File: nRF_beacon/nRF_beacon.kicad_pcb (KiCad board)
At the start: 2 copper layers, 22 parts, among them U1 nRF54L15-QFAA, U2 NPM1300-QEAA-R7, U3 MAX98357A, X1 32MHz

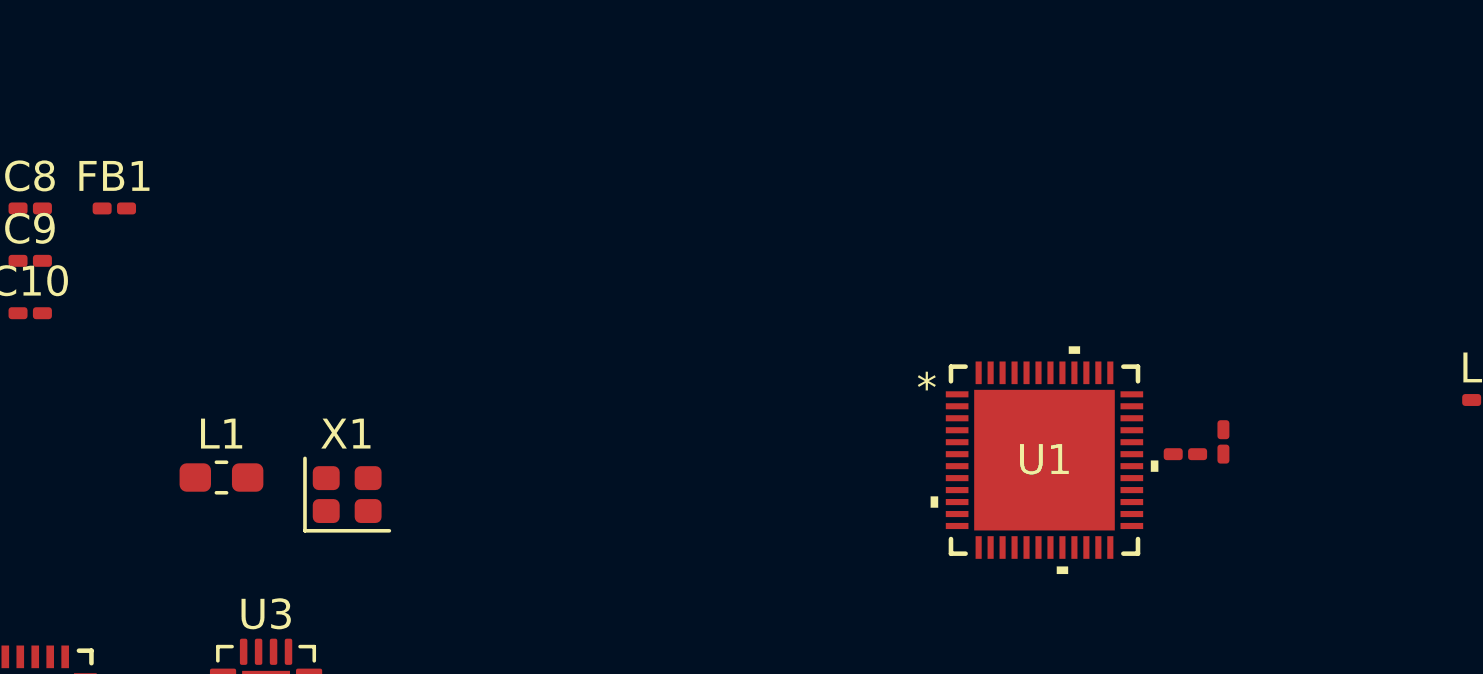
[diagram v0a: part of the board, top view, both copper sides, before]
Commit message: Updated nPM schematic. Added TWI and debug connector
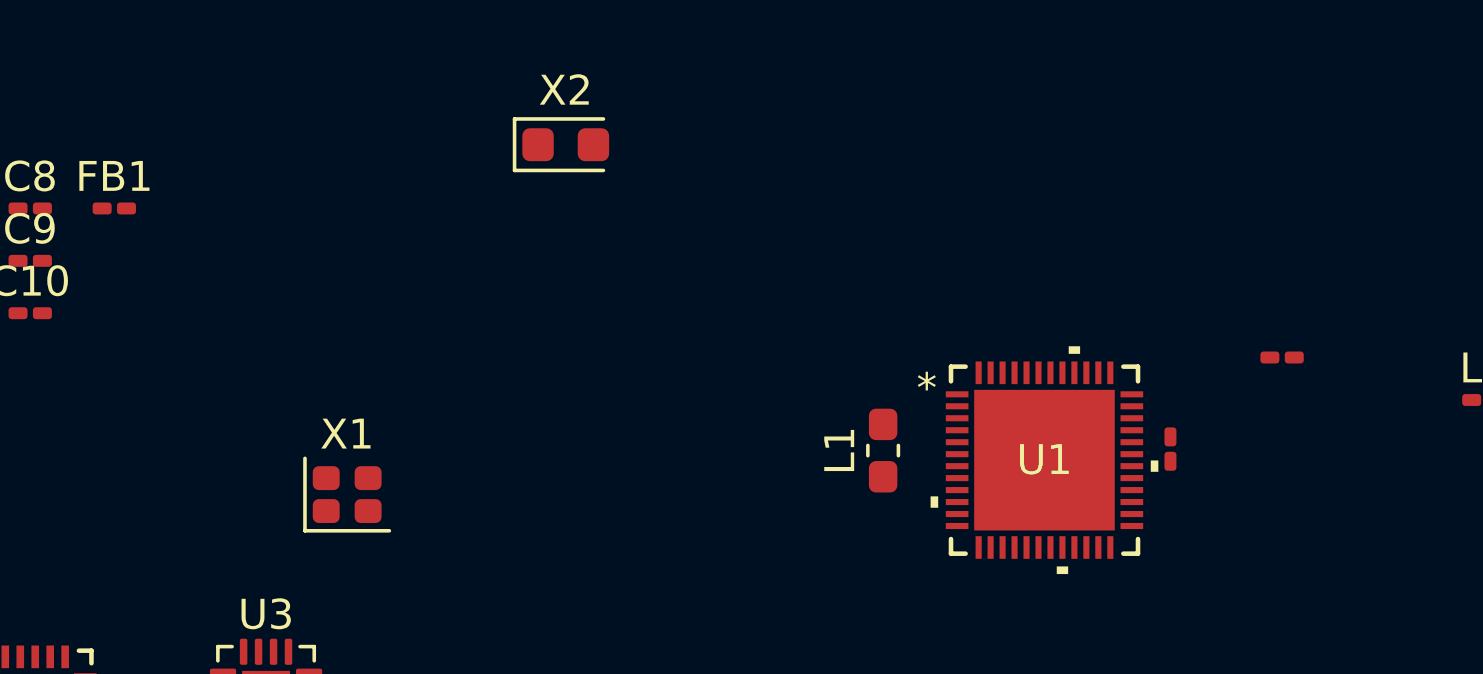
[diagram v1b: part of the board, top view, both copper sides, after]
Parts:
- added X2: 32.768 kHz, Crystal:Crystal_SMD_2012-2Pin_2.0x1.2mm_HandSoldering, F.Cu at (153.0, 64.5)
- moved L1 22.1 mm to (163.6, 74.7), turned to 90 degrees
- moved L2 4.57 mm to (176.9, 71.6)
- moved C11 1.79 mm to (173.2, 74.7)
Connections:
- net /~{SD_MODE} renamed Net-(U3-~{SD_MODE})
- net PVSS1 renamed Net-(U2-PVSS1)
- U1 pad 1: unconnected-(U1C-P1.00/XL1-Pad1) -> Net-(U1C-P1.00/XL1)
- U1 pad 2: unconnected-(U1C-P1.01/XL2-Pad2) -> Net-(U1C-P1.01/XL2)
- U1 pad 39: unconnected-(U1C-P1.11/AIN4/CK-Pad39) -> /MCU/SDA
- U1 pad 40: unconnected-(U1C-P1.12/AIN5/CK-Pad40) -> /MCU/SCL
- U1 pad 6: /DIN -> /LRCLK
- U1 pad 7: /LRCLK -> /DIN/DOUT
- U1 pad 8: /MCU/P1.07/AIN3 -> unconnected-(U1C-P1.07/AIN3-Pad8)
- U2 pad 1: VOUT1 -> VDD_AUDIO
- U2 pad 12: unconnected-(U2-VDDIO-Pad12) -> VDD_nRF
- U2 pad 13: unconnected-(U2-SDA-Pad13) -> /MCU/SDA
- U2 pad 14: unconnected-(U2-SCL-Pad14) -> /MCU/SCL
- U2 pad 21: /POWER/VBUS -> unconnected-(U2-VBUS-Pad21)
- U2 pad 23: /POWER/CC1 -> unconnected-(U2-CC1-Pad23)
- U2 pad 24: /POWER/CC2 -> unconnected-(U2-CC2-Pad24)
- U2 pad 29: (no net) -> unconnected-(U2-LSOUT1/VOUTLDO1-Pad29)
- U2 pad 32: unconnected-(U2-VOUT2-Pad32) -> VDD_nRF
- U2 pad 33: unconnected-(U2-AVSS-Pad33) -> Earth
- U2 pad 5: unconnected-(U2-SW2-Pad5) -> /POWER/SW2
- U2 pad 6: unconnected-(U2-PVSS2-Pad6) -> PVSS2
- U3 pad 1: /DIN -> /DIN/DOUT
- U3 pad 7: +5V -> VDD_AUDIO
- U3 pad 8: +5V -> VDD_AUDIO

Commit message: Finished first schematic draft. Ready for layout
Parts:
- added AE1: Antenna, Ekse:PCB_Antenna, F.Cu at (207.5, 61.6)
- added C14: 10uF, Capacitor_SMD:C_0603_1608Metric_Pad1.08x0.95mm_HandSolder, F.Cu at (149.5, 140.7)
- added C15: 2.2uF, Capacitor_SMD:C_0603_1608Metric_Pad1.08x0.95mm_HandSolder, F.Cu at (149.5, 143.2)
- added C16: 10uF, Capacitor_SMD:C_0603_1608Metric_Pad1.08x0.95mm_HandSolder, F.Cu at (149.5, 145.7)
- added C17: 10uF, Capacitor_SMD:C_0603_1608Metric_Pad1.08x0.95mm_HandSolder, F.Cu at (161.2, 140.7)
- added C18: 0.1uF, Capacitor_SMD:C_0201_0603Metric_Pad0.64x0.40mm_HandSolder, F.Cu at (164.8, 146.4)
- added C19: 220pF, Capacitor_SMD:C_0603_1608Metric_Pad1.08x0.95mm_HandSolder, F.Cu at (161.2, 143.2)
- added C20: 220pF, Capacitor_SMD:C_0603_1608Metric_Pad1.08x0.95mm_HandSolder, F.Cu at (161.2, 145.7)
- added C21: 0.1uF, Capacitor_SMD:C_0201_0603Metric_Pad0.64x0.40mm_HandSolder, F.Cu at (202.8, 129.2)
- added C22: 0.1uF, Capacitor_SMD:C_0201_0603Metric_Pad0.64x0.40mm_HandSolder, F.Cu at (153.1, 147.0)
- added C23: 10uF, Capacitor_SMD:C_0603_1608Metric_Pad1.08x0.95mm_HandSolder, F.Cu at (149.5, 148.3)
- added C24: 10uF, Capacitor_SMD:C_0603_1608Metric_Pad1.08x0.95mm_HandSolder, F.Cu at (149.5, 150.8)
- added C25: 10uF, Capacitor_SMD:C_0603_1608Metric_Pad1.08x0.95mm_HandSolder, F.Cu at (149.5, 153.3)
- added D1: LED_RGBA, Ekse:APGF1012GBRC07, F.Cu at (153.8, 153.5)
- added FB2: 1000, Capacitor_SMD:C_0805_2012Metric_Pad1.18x1.45mm_HandSolder, F.Cu at (165.8, 141.0)
- added FB3: 1000, Capacitor_SMD:C_0805_2012Metric_Pad1.18x1.45mm_HandSolder, F.Cu at (165.8, 144.0)
- added J1: Conn_02x05_Odd_Even, Ekse:FTSH-105-XX-YYY-DV-K-P-TR, F.Cu at (196.5, 123.6)
- added J2: Conn_02x03_Counter_Clockwise, Ekse:SAMTEC_TSM-103-01-L-DV-P-TR, F.Cu at (187.0, 124.3)
- added L5: 2.2uH, Ekse:INDC2016X100N, F.Cu at (153.9, 141.1)
- added L6: 2.2uH, Ekse:INDC2016X100N, F.Cu at (153.9, 144.5)
- added LS1: AS07104PO-R, Ekse:VN02A1500000G, F.Cu at (204.5, 123.4)
- added NT1: Net Tie, NetTie:NetTie-4_SMD_Pad0.5mm, F.Cu at (155.8, 147.4)
- added NT2: Net Tie, NetTie:NetTie-4_SMD_Pad0.5mm, F.Cu at (155.8, 149.9)
- added R1: 634k, Resistor_SMD:R_0603_1608Metric_Pad0.98x0.95mm_HandSolder, F.Cu at (161.2, 148.3)
- added R2: 1k, Resistor_SMD:R_0201_0603Metric_Pad0.64x0.40mm_HandSolder, F.Cu at (160.4, 152.4)
- added R3: 10k, Resistor_SMD:R_0603_1608Metric_Pad0.98x0.95mm_HandSolder, F.Cu at (149.5, 155.8)
- added R4: 10k, Resistor_SMD:R_0603_1608Metric_Pad0.98x0.95mm_HandSolder, F.Cu at (149.5, 158.3)
- added R5: 150k, Resistor_SMD:R_0201_0603Metric_Pad0.64x0.40mm_HandSolder, F.Cu at (153.1, 148.8)
- added R6: 150k, Resistor_SMD:R_0201_0603Metric_Pad0.64x0.40mm_HandSolder, F.Cu at (153.1, 150.5)
- added U4: 12BHC186P1-GR, Ekse:12BHC186P1GR, F.Cu at (192.3, 106.6)
- moved U1 25.8 mm to (190.8, 61.3)
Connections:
- U1 pad 37: unconnected-(U1C-P1.09-Pad37) -> /P1.09
- U1 pad 38: unconnected-(U1C-P1.10-Pad38) -> /P1.10
- U1 pad 41: unconnected-(U1C-P1.13/AIN6-Pad41) -> /P1.13
- U1 pad 42: unconnected-(U1C-P1.14/AIN7-Pad42) -> /P1.14
- U1 pad 8: unconnected-(U1C-P1.07/AIN3-Pad8) -> /P1.07
- U1 pad 9: unconnected-(U1C-P1.08/EXTREF/CLK16M/CK-Pad9) -> /P1.08
- U2 pad 16: unconnected-(U2-VSET2-Pad16) -> Net-(U2-VSET2)
- U2 pad 17: unconnected-(U2-VSET1-Pad17) -> Net-(U2-VSET1)
- U2 pad 18: /NTC -> unconnected-(U2-NTC-Pad18)
- U2 pad 20: unconnected-(U2-VSYS-Pad20) -> Net-(U2-PVDD)
- U2 pad 25: unconnected-(U2-LED0-Pad25) -> Net-(D1-BK)
- U2 pad 26: unconnected-(U2-LED1-Pad26) -> Net-(D1-GK)
- U2 pad 27: unconnected-(U2-LED2-Pad27) -> Net-(D1-RK)
- U2 pad 4: unconnected-(U2-PVDD-Pad4) -> Net-(U2-PVDD)
- U2 pad 6: PVSS2 -> Net-(U2-PVSS2)

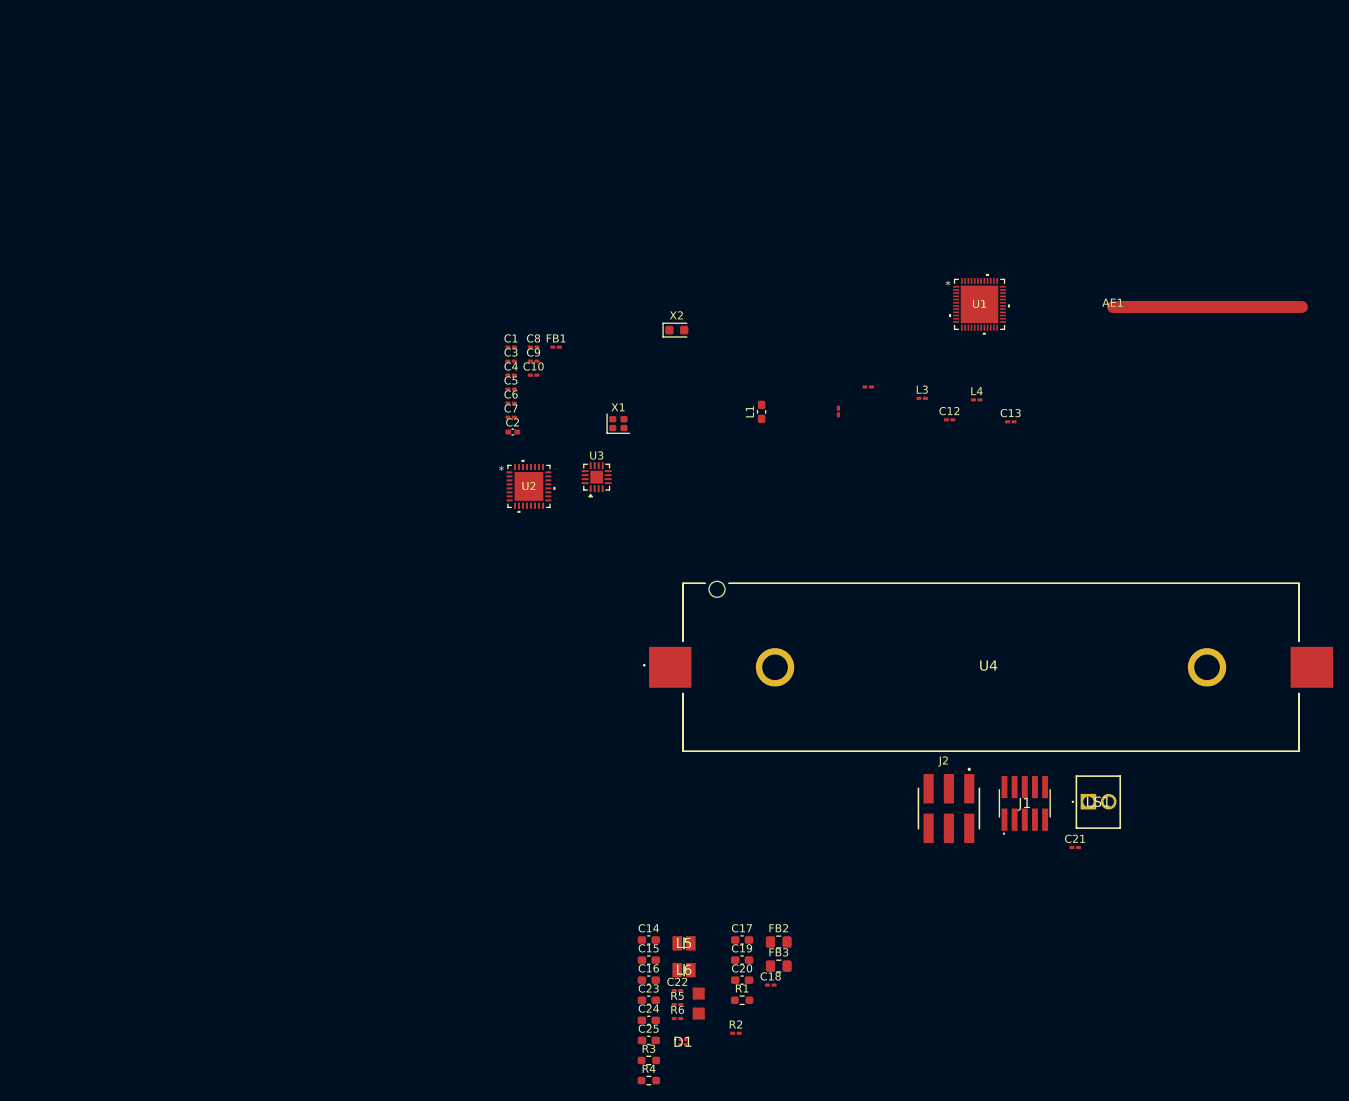
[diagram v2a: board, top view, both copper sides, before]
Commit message: Roughly grouped components by function in PCB-layout
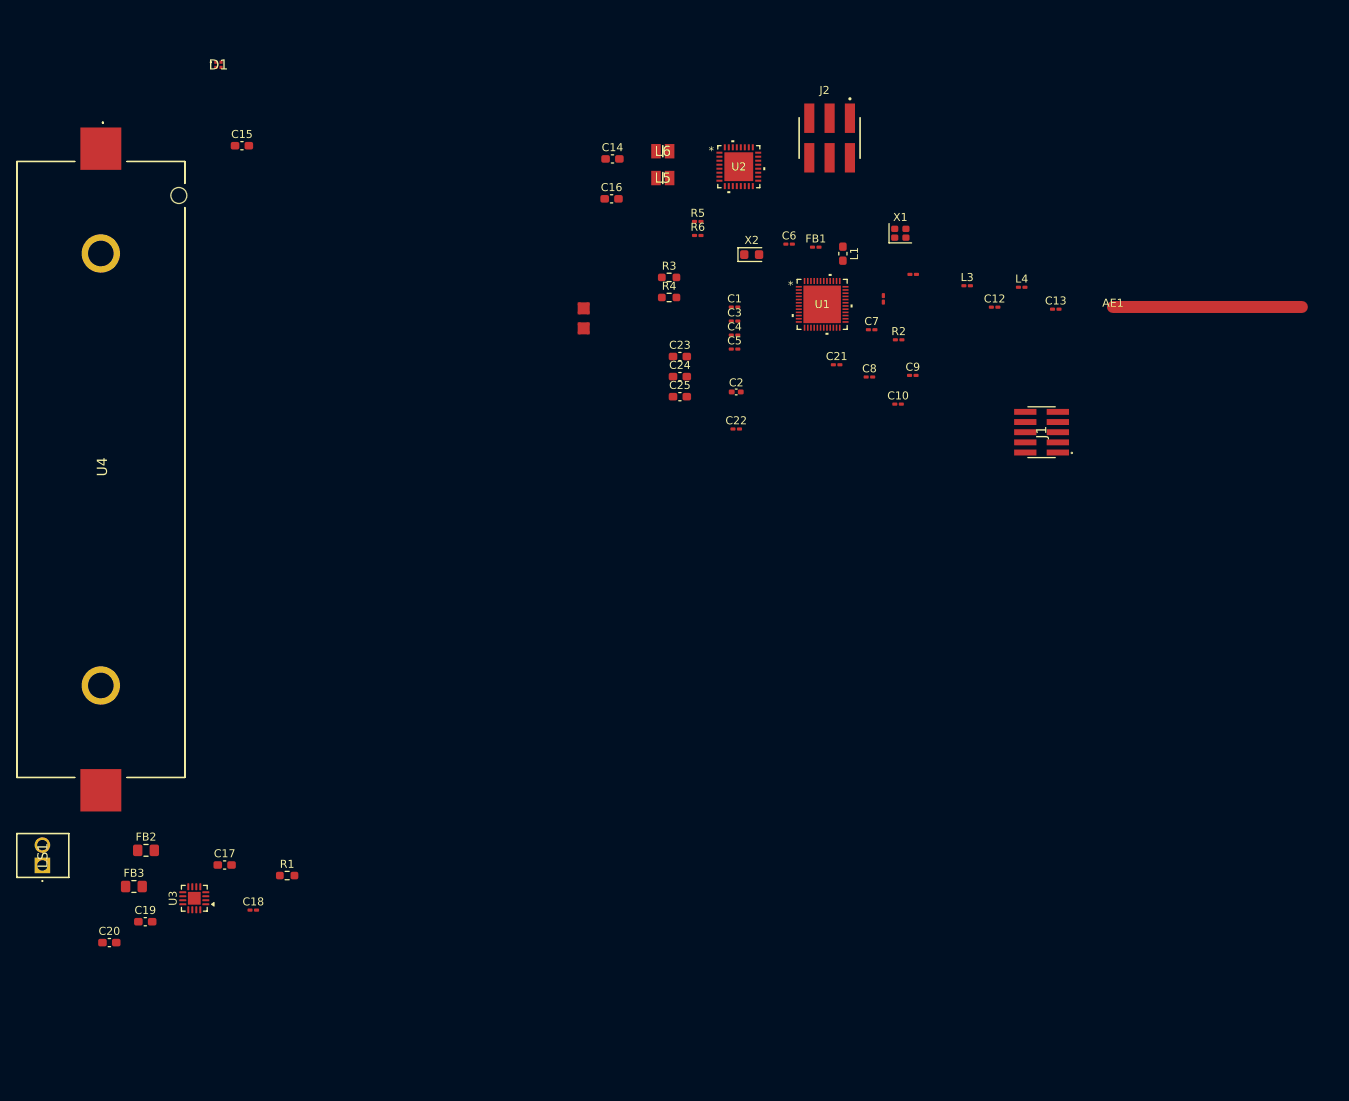
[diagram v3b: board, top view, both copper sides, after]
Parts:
- moved D1 135.3 mm to (95.7, 31.3)
- moved LS1 131.0 mm to (73.7, 131.4), turned to 90 degrees
- moved U4 114.0 mm to (81.0, 81.9), turned to -90 degrees
- moved C15 113.8 mm to (98.7, 41.4)
- moved L6 102.4 mm to (151.3, 42.1), turned to 180 degrees
- moved R3 97.9 mm to (152.1, 57.9)
- moved R4 97.9 mm to (152.1, 60.4)
- moved R5 97.9 mm to (155.6, 50.9)
- moved R6 97.9 mm to (155.6, 52.7)
- moved C16 97.8 mm to (144.9, 48.1)
- moved C14 97.7 mm to (145.0, 43.1)
- moved L5 95.7 mm to (151.3, 45.5), turned to 180 degrees
- moved R2 89.0 mm to (180.7, 65.7)
- moved NT2 86.8 mm to (141.4, 64.3)
- moved NT1 86.8 mm to (141.4, 61.8)
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
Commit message: Began matching network layout
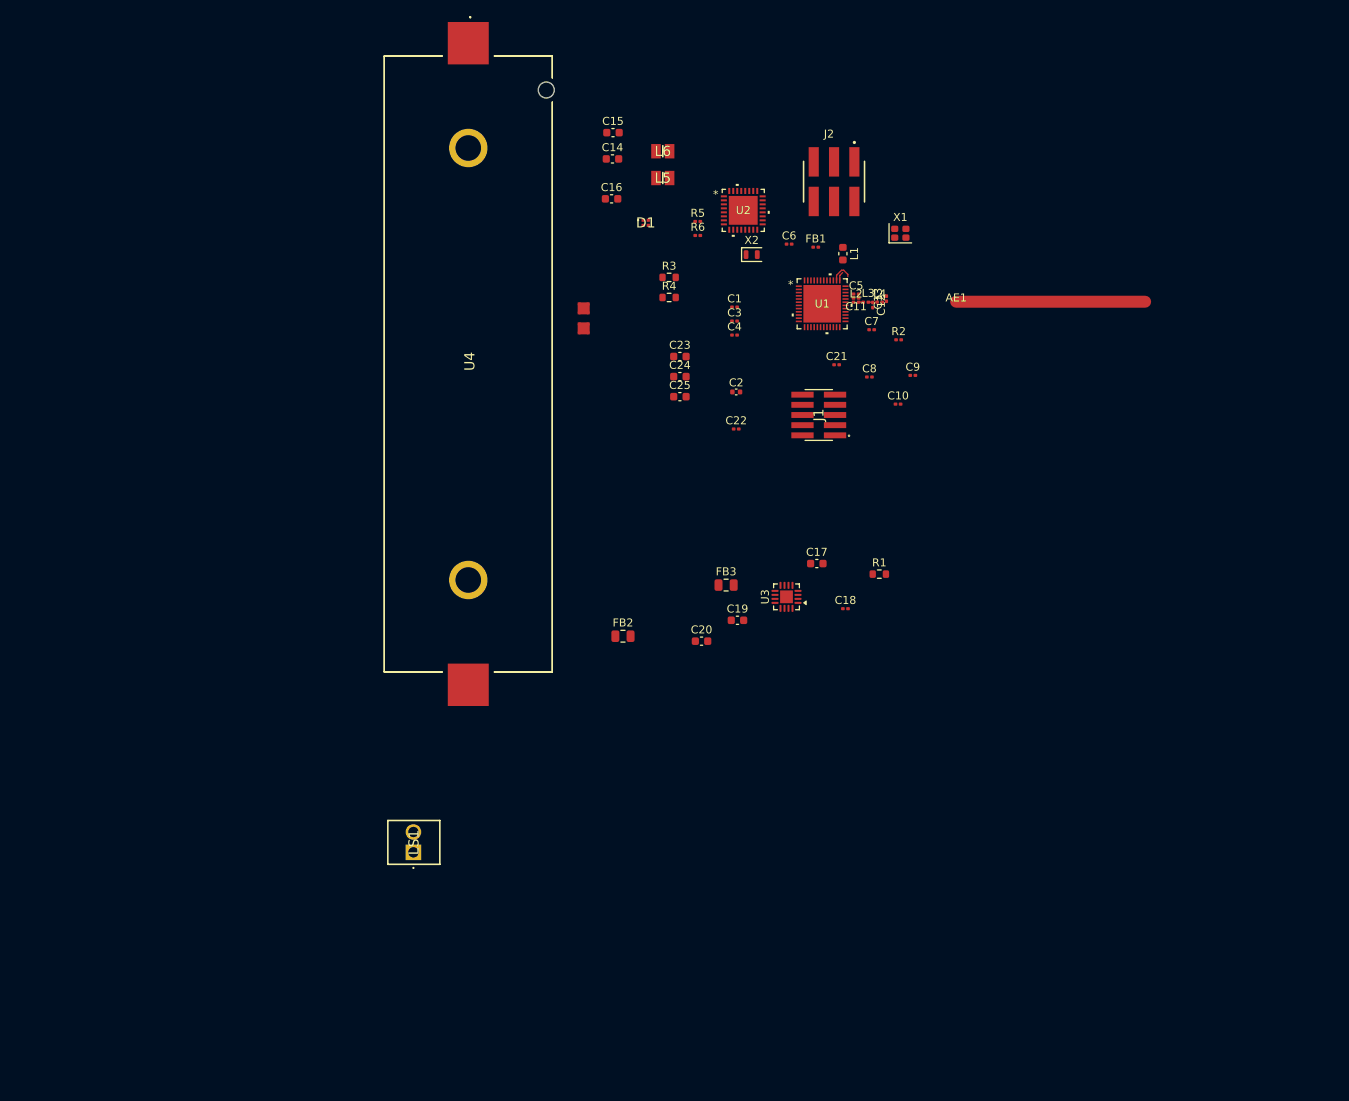
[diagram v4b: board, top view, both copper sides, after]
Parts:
- C1, C10, C11, C12, C13, C18, C21, C22, C3, C4, C5, C6, C7, C8, C9: footprint Capacitor_SMD:C_0201_0603Metric_Pad0.64x0.40mm_HandSolder -> Capacitor_SMD:C_0201_0603Metric
- C14, C15, C16, C17, C19, C20, C23, C24, C25: footprint Capacitor_SMD:C_0603_1608Metric_Pad1.08x0.95mm_HandSolder -> Capacitor_SMD:C_0603_1608Metric
- C2: footprint Capacitor_SMD:C_0402_1005Metric_Pad0.74x0.62mm_HandSolder -> Capacitor_SMD:C_0402_1005Metric
- FB1, L2, L3, L4: footprint Inductor_SMD:L_0201_0603Metric_Pad0.64x0.40mm_HandSolder -> Inductor_SMD:L_0201_0603Metric
- FB2, FB3: footprint Capacitor_SMD:C_0805_2012Metric_Pad1.18x1.45mm_HandSolder -> Capacitor_SMD:C_0805_2012Metric
- L1: footprint Inductor_SMD:L_0603_1608Metric_Pad1.05x0.95mm_HandSolder -> Inductor_SMD:L_0603_1608Metric
- R1, R3, R4: footprint Resistor_SMD:R_0603_1608Metric_Pad0.98x0.95mm_HandSolder -> Resistor_SMD:R_0603_1608Metric
- R2, R5, R6: footprint Resistor_SMD:R_0201_0603Metric_Pad0.64x0.40mm_HandSolder -> Resistor_SMD:R_0201_0603Metric
- X2: footprint Crystal:Crystal_SMD_2012-2Pin_2.0x1.2mm_HandSoldering -> Crystal:Crystal_SMD_2012-2Pin_2.0x1.2mm
- moved C18 83.1 mm to (174.1, 99.3)
- moved C19 83.1 mm to (160.6, 100.8)
- moved C20 83.1 mm to (156.1, 103.4)
- moved FB3 83.1 mm to (159.2, 96.4)
- moved C17 83.1 mm to (170.5, 93.7)
- moved R1 83.1 mm to (178.3, 95.0)
- moved U3 83.1 mm to (166.9, 97.8)
- moved FB2 65.4 mm to (146.3, 102.8)
- moved D1 56.9 mm to (149.1, 51.1)
- moved U4 47.8 mm to (126.9, 68.7)
- moved LS1 46.4 mm to (120.1, 129.8)
- moved C15 46.4 mm to (145.0, 39.8)
- moved J1 27.9 mm to (170.8, 75.1)
- moved C13 21.2 mm to (179.2, 60.6), turned to 90 degrees
- moved AE1 19.6 mm to (187.9, 60.9)
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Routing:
- net /P1.10: track 0.00 -> 2.82 mm
- net /P1.09: track 0.00 -> 1.13 mm
- net Net-(C12-Pad1): track 0.00 -> 1.12 mm
- net Net-(C11-Pad1): track 0.00 -> 0.57 mm
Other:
- copper layers 2 -> 4
